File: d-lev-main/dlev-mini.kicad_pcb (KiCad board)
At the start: 4 copper layers, 171.4 x 146.7 mm, 84 parts, among them J1 Conn_01x12_MountingPin, J2 Tag-Connect TC2030-NL, J3 S8B-PH-SM4-TB, J4 S8B-PH-SM4-TB, J5 Conn_01x06_MountingPin, Q2 MMBT3904, Q3 BSS138, Q4 BSS138, Q5 BSS138, SW1 RotaryEncoder_Switch, SW2 RotaryEncoder_Switch, SW3 RotaryEncoder_Switch, SW4 RotaryEncoder_Switch, SW5 RotaryEncoder_Switch, SW6 RotaryEncoder_Switch, SW7 RotaryEncoder_Switch, SW8 RotaryEncoder_Switch, U1 25LCxxx, U2 AMS1117-3.3, U3 AC608

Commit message: many changes to pcb
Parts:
- C10: value .1u -> .01u; footprint Capacitor_SMD:C_0805_2012Metric_Pad1.18x1.45mm_HandSolder -> Capacitor_SMD:C_0603_1608Metric
- C17, C18: value .01u -> 22u; footprint Capacitor_SMD:C_0603_1608Metric -> Capacitor_SMD:C_0805_2012Metric_Pad1.18x1.45mm_HandSolder
- C21: value .01u -> .1u; footprint Capacitor_SMD:C_0603_1608Metric -> Capacitor_SMD:C_0805_2012Metric_Pad1.18x1.45mm_HandSolder
- C7, C8: value 22u -> .01u; footprint Capacitor_SMD:C_0805_2012Metric_Pad1.18x1.45mm_HandSolder -> Capacitor_SMD:C_0603_1608Metric
- DS2: value LCD-20X4B -> LCD-20X4B-noshield
- moved H4 245.4 mm to (-75.5, -98.2)
- moved J2 222.9 mm to (5.00, -106.0), turned to 180 degrees
- moved U1 207.6 mm to (35.0, -67.0), turned to 45 degrees
- moved RV1 199.2 mm to (-54.2, -97.6), turned to 90 degrees
- moved H3 189.3 mm to (75.5, -98.2)
- moved C19 170.9 mm to (-24.0, 104.1)
- moved C9 169.6 mm to (76.0, -44.3)
- moved U2 167.9 mm to (-23.0, -29.0), turned to -135 degrees
- moved C8 166.1 mm to (-41.2, 18.0), turned to 180 degrees
- moved C7 155.7 mm to (-30.3, 18.0)
- moved RN7 153.2 mm to (70.6, -9.95), turned to 90 degrees
- moved C11 152.4 mm to (41.0, -17.0)
- moved H2 144.6 mm to (-75.5, 40.8)
- moved C6 140.7 mm to (-76.0, -9.25), turned to 180 degrees
- moved RN3 139.0 mm to (-70.5, -9.96), turned to 90 degrees
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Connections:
- C10 pad 1: Net-(C10-Pad1) -> enc_6.b
- C11 pad 1: /spdif_tx_1 -> enc_5.a
- C11 pad 2: Net-(C11-Pad2) -> GND
- C12 pad 1: enc_6.a -> enc_5.b
- C13 pad 1: enc_6.b -> enc_7.a
- C14 pad 1: enc_5.a -> enc_7.b
- C15 pad 1: enc_5.b -> enc_8.a
- C16 pad 1: enc_7.a -> enc_8.b
- C17 pad 1: enc_7.b -> +3V3
- C18 pad 1: enc_1.a -> +5V
- C19 pad 1: enc_1.b -> /spdif_tx_1
- C19 pad 2: GND -> Net-(C19-Pad2)
- C20 pad 1: enc_8.a -> /spdif_tx_0
- C20 pad 2: GND -> Net-(C20-Pad2)
- C21 pad 1: enc_8.b -> Net-(C21-Pad1)
- C3 pad 1: enc_3.a -> enc_1.a
- C4 pad 1: enc_3.b -> enc_1.b
- C5 pad 1: enc_4.a -> enc_3.a
- C6 pad 1: enc_4.b -> enc_3.b
- C7 pad 1: +3V3 -> enc_4.a
- C8 pad 1: +5V -> enc_4.b
- C9 pad 1: /spdif_tx_0 -> enc_6.a
- C9 pad 2: Net-(C9-Pad2) -> GND
- R10 pad 1: Net-(C11-Pad2) -> Net-(C19-Pad2)
- R5 pad 1: Net-(C10-Pad1) -> Net-(C21-Pad1)
- R7 pad 2: Net-(C10-Pad1) -> Net-(C21-Pad1)
- R8 pad 2: Net-(C10-Pad1) -> Net-(C21-Pad1)
- R9 pad 1: Net-(C9-Pad2) -> Net-(C20-Pad2)
- RN2 pad 1: /encoder2/B1 -> /encoder/B1
- RN2 pad 2: /encoder2/A1 -> /encoder/A1
- RN2 pad 3: /encoder2/A1 -> /encoder/A1
- RN2 pad 4: /encoder2/B1 -> /encoder/B1
- RN2 pad 7: enc_3.a -> enc_1.a
- RN2 pad 8: enc_3.b -> enc_1.b
- RN3 pad 1: /encoder3/B1 -> /encoder2/B1
- RN3 pad 2: /encoder3/A1 -> /encoder2/A1
- RN3 pad 3: /encoder3/A1 -> /encoder2/A1
- RN3 pad 4: /encoder3/B1 -> /encoder2/B1
- RN3 pad 7: enc_4.a -> enc_3.a
- RN3 pad 8: enc_4.b -> enc_3.b
- RN4 pad 1: /encoder4/B1 -> /encoder3/B1
- RN4 pad 2: /encoder4/A1 -> /encoder3/A1
- RN4 pad 3: /encoder4/A1 -> /encoder3/A1
- RN4 pad 4: /encoder4/B1 -> /encoder3/B1
- RN4 pad 7: enc_6.a -> enc_4.a
- RN4 pad 8: enc_6.b -> enc_4.b
- RN5 pad 1: /encoder7/B1 -> /encoder4/B1
- RN5 pad 2: /encoder7/A1 -> /encoder4/A1
- RN5 pad 3: /encoder7/A1 -> /encoder4/A1
- RN5 pad 4: /encoder7/B1 -> /encoder4/B1
- RN5 pad 7: enc_5.a -> enc_6.a
- RN5 pad 8: enc_5.b -> enc_6.b
- RN6 pad 1: /encoder5/B1 -> /encoder7/B1
- RN6 pad 2: /encoder5/A1 -> /encoder7/A1
- RN6 pad 3: /encoder5/A1 -> /encoder7/A1
- RN6 pad 4: /encoder5/B1 -> /encoder7/B1
- RN6 pad 7: enc_7.a -> enc_5.a
- RN6 pad 8: enc_7.b -> enc_5.b
- RN7 pad 1: /encoder/B1 -> /encoder5/B1
- RN7 pad 2: /encoder/A1 -> /encoder5/A1
- RN7 pad 3: /encoder/A1 -> /encoder5/A1
- RN7 pad 4: /encoder/B1 -> /encoder5/B1
- RN7 pad 7: enc_1.a -> enc_7.a
- RN7 pad 8: enc_1.b -> enc_7.b
- U3 pad 1: (no net) -> unconnected-(U3-IO_T14-Pad1)
- U3 pad 10: (no net) -> unconnected-(U3-IO_L15-Pad10)
- U3 pad 100: (no net) -> unconnected-(U3-IO_R3-Pad100)
- U3 pad 101: (no net) -> unconnected-(U3-IO_T3-Pad101)
- U3 pad 102: (no net) -> unconnected-(U3-IO_R4-Pad102)
- U3 pad 103: (no net) -> unconnected-(U3-IO_T4-Pad103)
- U3 pad 104: (no net) -> unconnected-(U3-IO_R5-Pad104)
- U3 pad 105: (no net) -> unconnected-(U3-IO_T5-Pad105)
- U3 pad 106: (no net) -> +3V3
- U3 pad 107: (no net) -> GND
- U3 pad 108: (no net) -> unconnected-(U3-IO_R6-Pad108)
- U3 pad 109: (no net) -> unconnected-(U3-IO_T6-Pad109)
- U3 pad 11: (no net) -> unconnected-(U3-IO_L16-Pad11)
- U3 pad 110: (no net) -> unconnected-(U3-IO_R7-Pad110)
- U3 pad 111: (no net) -> unconnected-(U3-IO_T7-Pad111)
- U3 pad 112: (no net) -> unconnected-(U3-I_R8-Pad112)
- U3 pad 113: (no net) -> unconnected-(U3-I_T8-Pad113)
- U3 pad 114: (no net) -> unconnected-(U3-I_R9-Pad114)
- U3 pad 115: (no net) -> unconnected-(U3-I_T9-Pad115)
- U3 pad 116: (no net) -> unconnected-(U3-IO_R10-Pad116)
- U3 pad 117: (no net) -> unconnected-(U3-IO_T10-Pad117)
- U3 pad 118: (no net) -> unconnected-(U3-IO_R11-Pad118)
- U3 pad 119: (no net) -> unconnected-(U3-IO_T11-Pad119)
- U3 pad 12: (no net) -> unconnected-(U3-IO_P11-Pad12)
- U3 pad 120: (no net) -> unconnected-(U3-IO_R12-Pad120)
- U3 pad 121: (no net) -> unconnected-(U3-IO_T12-Pad121)
- U3 pad 122: (no net) -> unconnected-(U3-IO_R13-Pad122)
- U3 pad 123: (no net) -> unconnected-(U3-IO_T13-Pad123)
- U3 pad 124: (no net) -> unconnected-(U3-IO_R14-Pad124)
- U3 pad 13: (no net) -> unconnected-(U3-IO_N11-Pad13)
- U3 pad 14: (no net) -> +3V3
- U3 pad 15: (no net) -> GND
- U3 pad 16: (no net) -> unconnected-(U3-IO_N12-Pad16)
- U3 pad 17: (no net) -> unconnected-(U3-IO_P14-Pad17)
- U3 pad 18: (no net) -> unconnected-(U3-IO_N14-Pad18)
- U3 pad 19: (no net) -> unconnected-(U3-IO_L13-Pad19)
- U3 pad 2: (no net) -> unconnected-(U3-IO_T15-Pad2)
- U3 pad 20: (no net) -> unconnected-(U3-IO_K16-Pad20)
- U3 pad 21: (no net) -> unconnected-(U3-IO_J15-Pad21)
- U3 pad 22: (no net) -> unconnected-(U3-IO_J16-Pad22)
- U3 pad 23: (no net) -> unconnected-(U3-IO_L14-Pad23)
- U3 pad 24: (no net) -> unconnected-(U3-IO_J14-Pad24)
- U3 pad 25: (no net) -> unconnected-(U3-IO_K15-Pad25)
- U3 pad 26: (no net) -> unconnected-(U3-IO_F16-Pad26)
- U3 pad 27: (no net) -> unconnected-(U3-IO_G15-Pad27)
- U3 pad 28: (no net) -> unconnected-(U3-IO_F15-Pad28)
- U3 pad 29: (no net) -> unconnected-(U3-I_E16-Pad29)
- U3 pad 3: (no net) -> unconnected-(U3-IO_R16-Pad3)
- U3 pad 30: (no net) -> unconnected-(U3-IO_D16-Pad30)
- U3 pad 31: (no net) -> unconnected-(U3-IO_D15-Pad31)
- U3 pad 32: (no net) -> unconnected-(U3-IO_C16-Pad32)
- U3 pad 33: (no net) -> unconnected-(U3-IO_C15-Pad33)
- U3 pad 34: (no net) -> unconnected-(U3-IO_B16-Pad34)
- U3 pad 35: (no net) -> unconnected-(U3-IO_J13-Pad35)
- U3 pad 36: (no net) -> unconnected-(U3-IO_G16-Pad36)
- U3 pad 37: (no net) -> unconnected-(U3-IO_F8-Pad37)
- U3 pad 38: (no net) -> unconnected-(U3-IO_F13-Pad38)
- U3 pad 39: (no net) -> unconnected-(U3-IO_F14-Pad39)
- U3 pad 4: (no net) -> unconnected-(U3-IO_P15-Pad4)
- U3 pad 40: (no net) -> unconnected-(U3-IO_F9-Pad40)
- U3 pad 41: (no net) -> unconnected-(U3-IO_E11-Pad41)
- U3 pad 42: (no net) -> unconnected-(U3-I_A9-Pad42)
- U3 pad 43: (no net) -> unconnected-(U3-I_B9-Pad43)
- U3 pad 44: (no net) -> unconnected-(U3-IO_C9-Pad44)
- U3 pad 45: (no net) -> unconnected-(U3-I_A8-Pad45)
- U3 pad 46: (no net) -> unconnected-(U3-IO_D9-Pad46)
- U3 pad 47: (no net) -> unconnected-(U3-I_B8-Pad47)
- U3 pad 48: (no net) -> +3V3
- U3 pad 49: (no net) -> GND
- U3 pad 5: (no net) -> unconnected-(U3-IO_P16-Pad5)
- U3 pad 50: (no net) -> unconnected-(U3-I_E1-Pad50)
- U3 pad 51: (no net) -> unconnected-(U3-IO_B1-Pad51)
- U3 pad 52: (no net) -> unconnected-(U3-IO_C2-Pad52)
- U3 pad 53: (no net) -> unconnected-(U3-IO_D1-Pad53)
- U3 pad 54: (no net) -> unconnected-(U3-IO_F3-Pad54)
- U3 pad 55: (no net) -> unconnected-(U3-IO_F2-Pad55)
- U3 pad 56: (no net) -> unconnected-(U3-IO_F1-Pad56)
- U3 pad 57: (no net) -> unconnected-(U3-IO_G5-Pad57)
- U3 pad 58: (no net) -> unconnected-(U3-IO_G2-Pad58)
- U3 pad 59: (no net) -> unconnected-(U3-IO_G1-Pad59)
- U3 pad 6: (no net) -> unconnected-(U3-IO_N15-Pad6)
- U3 pad 60: (no net) -> /FPGA/TCK
- U3 pad 61: (no net) -> /FPGA/TDI
- U3 pad 62: (no net) -> /FPGA/TMS
- U3 pad 63: (no net) -> +2V5
- U3 pad 64: (no net) -> /FPGA/TDO
- U3 pad 65: (no net) -> unconnected-(U3-IO_K5-Pad65)
- U3 pad 66: (no net) -> unconnected-(U3-IO_L4-Pad66)
- U3 pad 67: (no net) -> unconnected-(U3-IO_M6-Pad67)
- U3 pad 68: (no net) -> unconnected-(U3-IO_N3-Pad68)
- U3 pad 69: (no net) -> unconnected-(U3-IO_N5-Pad69)
- U3 pad 7: (no net) -> unconnected-(U3-IO_N16-Pad7)
- U3 pad 70: (no net) -> unconnected-(U3-IO_P3-Pad70)
- U3 pad 71: (no net) -> unconnected-(U3-IO_L7-Pad71)
- U3 pad 72: (no net) -> unconnected-(U3-IO_N6-Pad72)
- U3 pad 73: (no net) -> GND
- U3 pad 74: (no net) -> +1V2
- U3 pad 75: (no net) -> unconnected-(U3-IO_P6-Pad75)
- U3 pad 76: (no net) -> unconnected-(U3-IO_M7-Pad76)
- U3 pad 77: (no net) -> unconnected-(U3-IO_M8-Pad77)
- U3 pad 78: (no net) -> +3V3
- U3 pad 79: (no net) -> GND
- U3 pad 8: (no net) -> unconnected-(U3-I_M15-Pad8)
- U3 pad 80: (no net) -> unconnected-(U3-IO_P8-Pad80)
- U3 pad 81: (no net) -> unconnected-(U3-IO_N8-Pad81)
- U3 pad 82: (no net) -> unconnected-(U3-IO_L8-Pad82)
- U3 pad 83: (no net) -> unconnected-(U3-IO_N9-Pad83)
- U3 pad 84: (no net) -> unconnected-(U3-IO_P9-Pad84)
- U3 pad 85: (no net) -> unconnected-(U3-IO_M10-Pad85)
- U3 pad 86: (no net) -> unconnected-(U3-LVDS_TX1_N-Pad86)
- U3 pad 87: (no net) -> unconnected-(U3-LVDS_TX1_P-Pad87)
- U3 pad 88: (no net) -> unconnected-(U3-LVDS_TX2_N-Pad88)
- U3 pad 89: (no net) -> unconnected-(U3-LVDS_TX2_P-Pad89)
- U3 pad 9: (no net) -> unconnected-(U3-I_M16-Pad9)
- U3 pad 90: (no net) -> unconnected-(U3-LVDS_TX3_N-Pad90)
- U3 pad 91: (no net) -> unconnected-(U3-LVDS_TX3_P-Pad91)
- U3 pad 92: (no net) -> unconnected-(U3-LVDS_RXCLK_N-Pad92)
- U3 pad 93: (no net) -> unconnected-(U3-LVDS_RXCLK_P-Pad93)
- U3 pad 94: (no net) -> unconnected-(U3-LVDS_TX4_N-Pad94)
- U3 pad 95: (no net) -> unconnected-(U3-LVDS_TX4_P-Pad95)
- U3 pad 96: (no net) -> unconnected-(U3-LVDS_TX5_N-Pad96)
- U3 pad 97: (no net) -> unconnected-(U3-LVDS_TX5_P-Pad97)
- U3 pad 98: (no net) -> unconnected-(U3-IO_R1-Pad98)
- U3 pad 99: (no net) -> unconnected-(U3-IO_T2-Pad99)
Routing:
- net /encoder3/B1: track 0.00 -> 9.17 mm
- net /encoder5/B1: track 0.00 -> 9.17 mm
- net /encoder/B1: track 0.00 -> 9.17 mm
- net /encoder4/B1: track 0.00 -> 9.17 mm
- net /encoder2/B1: track 0.00 -> 9.17 mm
- net /encoder6/B1: track 0.00 -> 9.17 mm
- net /encoder7/B1: track 0.00 -> 9.17 mm
- net enc_8.a: track 0.00 -> 6.72 mm
- net enc_5.a: track 0.00 -> 6.72 mm
- net enc_6.a: track 0.00 -> 6.72 mm
- net enc_4.a: track 0.00 -> 6.72 mm
- net enc_3.a: track 0.00 -> 6.72 mm
- net enc_7.a: track 0.00 -> 6.72 mm
- net enc_1.a: track 0.00 -> 6.72 mm
- net /encoder2/A1: track 0.00 -> 6.46 mm
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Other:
- board size 171.4 x 146.7 mm -> 175.3 x 163.3 mm

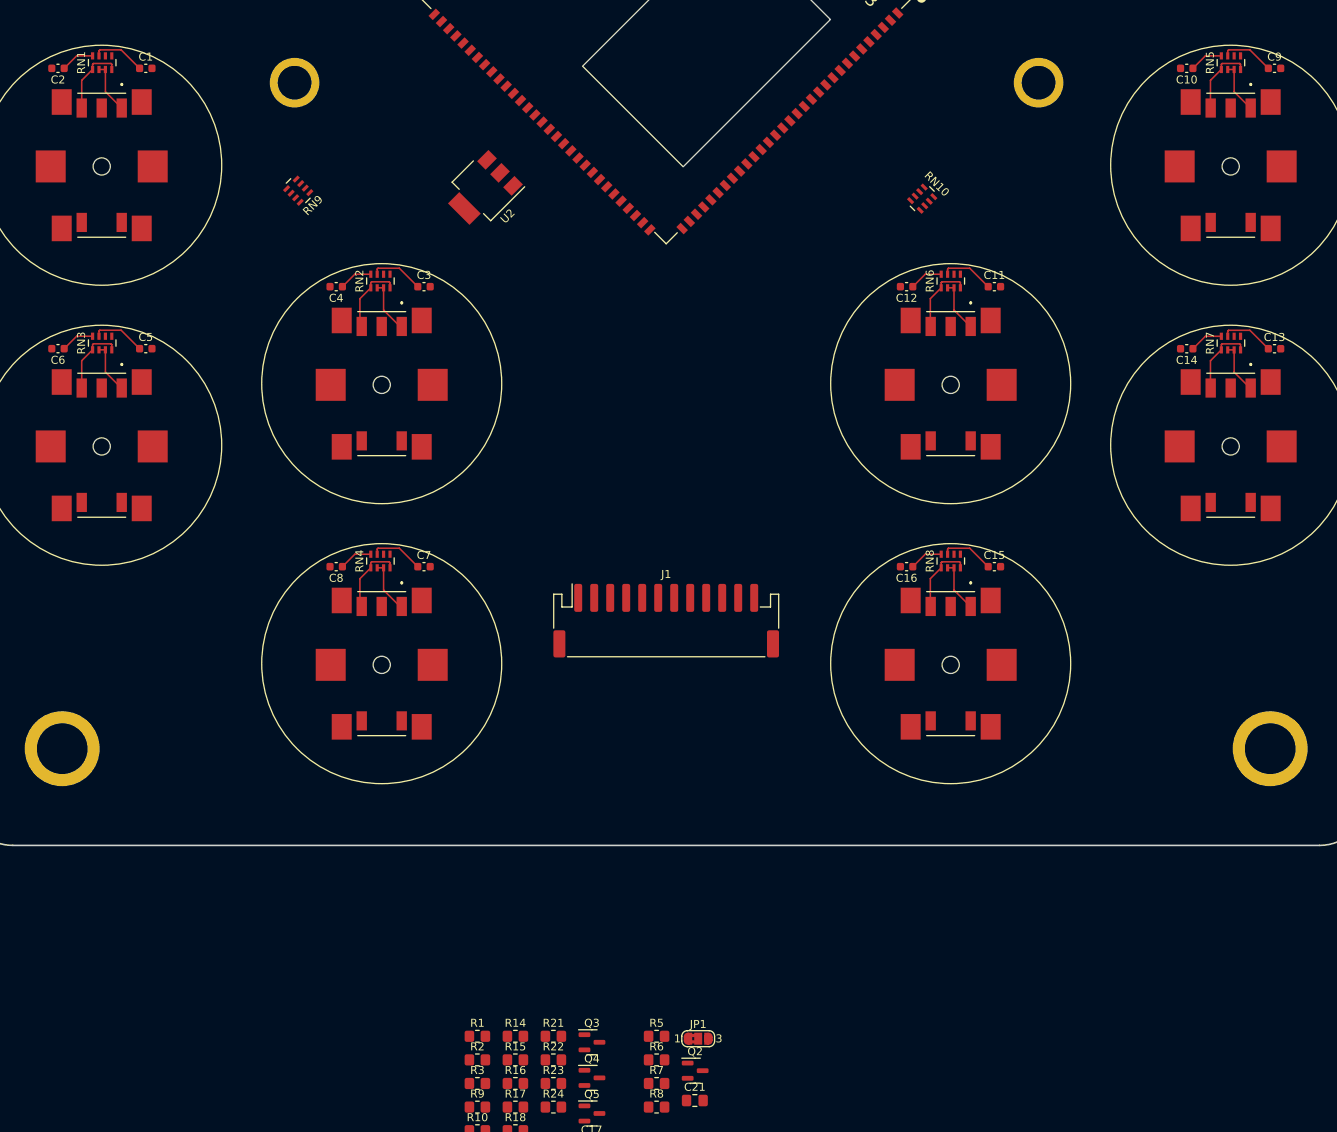
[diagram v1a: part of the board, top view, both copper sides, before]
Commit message: Switch from Rpacks to 0603 pull resistors
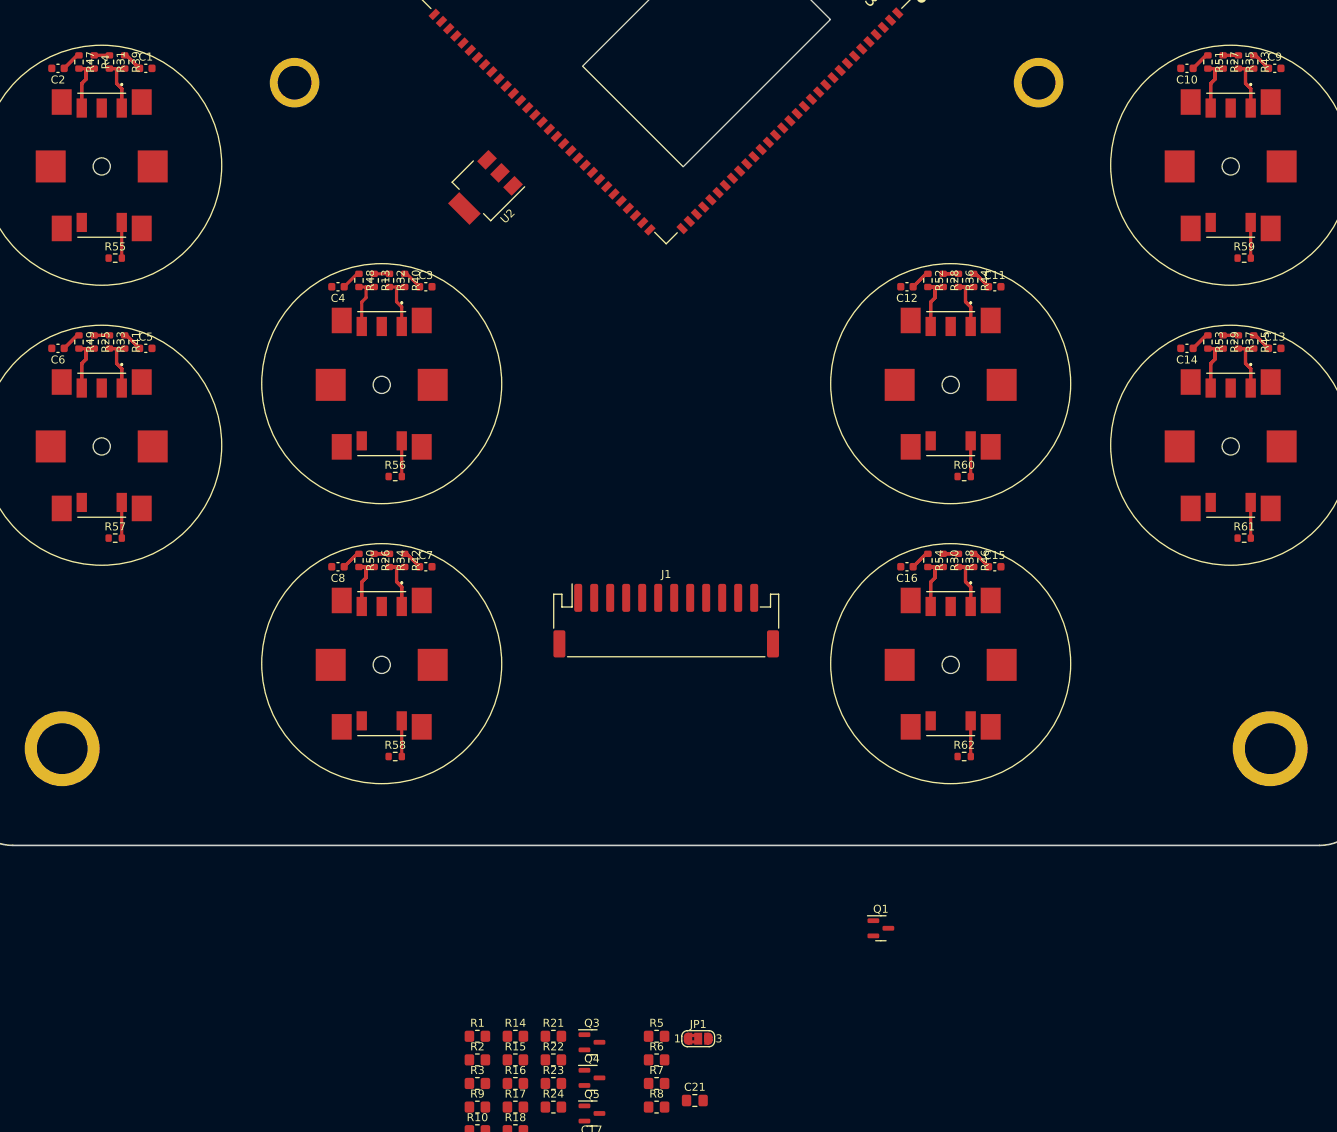
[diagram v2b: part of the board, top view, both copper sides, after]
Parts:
- removed Q2: MMBT3904, Package_TO_SOT_SMD:SOT-23
- removed RN1, RN10, RN2, RN3, RN4, RN5, RN6, RN7, RN8, RN9: 4.7k, Resistor_SMD:R_Array_Concave_4x0603
- added Q1: BSS138, Package_TO_SOT_SMD:SOT-23, F.Cu at (26.8, 63.2)
- added R13: R_Small, Resistor_SMD:R_0603_1608Metric, F.Cu at (-36.5, -17.8)
- added R25: R_Small, Resistor_SMD:R_0603_1608Metric, F.Cu at (-71.5, -10.1)
- added R26: R_Small, Resistor_SMD:R_0603_1608Metric, F.Cu at (-36.5, 17.2)
- added R27: R_Small, Resistor_SMD:R_0603_1608Metric, F.Cu at (69.6, -45.1)
- added R28: R_Small, Resistor_SMD:R_0603_1608Metric, F.Cu at (34.6, -17.8)
- added R29: R_Small, Resistor_SMD:R_0603_1608Metric, F.Cu at (69.6, -10.1)
- added R30: R_Small, Resistor_SMD:R_0603_1608Metric, F.Cu at (34.6, 17.2)
- added R31: R_Small, Resistor_SMD:R_0603_1608Metric, F.Cu at (-69.6, -45.1)
- added R32: R_Small, Resistor_SMD:R_0603_1608Metric, F.Cu at (-34.6, -17.8)
- added R33: R_Small, Resistor_SMD:R_0603_1608Metric, F.Cu at (-69.6, -10.1)
- added R34: R_Small, Resistor_SMD:R_0603_1608Metric, F.Cu at (-34.6, 17.2)
- added R35: R_Small, Resistor_SMD:R_0603_1608Metric, F.Cu at (71.5, -45.1)
- added R36: R_Small, Resistor_SMD:R_0603_1608Metric, F.Cu at (36.5, -17.8)
- added R37: R_Small, Resistor_SMD:R_0603_1608Metric, F.Cu at (71.5, -10.1)
- added R38: R_Small, Resistor_SMD:R_0603_1608Metric, F.Cu at (36.5, 17.2)
- added R39: R_Small, Resistor_SMD:R_0603_1608Metric, F.Cu at (-67.7, -45.1)
- added R4: R_Small, Resistor_SMD:R_0603_1608Metric, F.Cu at (-71.5, -45.1)
- added R40: R_Small, Resistor_SMD:R_0603_1608Metric, F.Cu at (-32.7, -17.8)
- added R41: R_Small, Resistor_SMD:R_0603_1608Metric, F.Cu at (-67.7, -10.1)
- added R42: R_Small, Resistor_SMD:R_0603_1608Metric, F.Cu at (-32.7, 17.2)
- added R43: R_Small, Resistor_SMD:R_0603_1608Metric, F.Cu at (73.4, -45.1)
- added R44: R_Small, Resistor_SMD:R_0603_1608Metric, F.Cu at (38.4, -17.8)
- added R45: R_Small, Resistor_SMD:R_0603_1608Metric, F.Cu at (73.4, -10.1)
- added R46: R_Small, Resistor_SMD:R_0603_1608Metric, F.Cu at (38.4, 17.2)
- added R47: R_Small, Resistor_SMD:R_0603_1608Metric, F.Cu at (-73.4, -45.1)
- added R48: R_Small, Resistor_SMD:R_0603_1608Metric, F.Cu at (-38.4, -17.8)
- added R49: R_Small, Resistor_SMD:R_0603_1608Metric, F.Cu at (-73.4, -10.1)
- added R50: R_Small, Resistor_SMD:R_0603_1608Metric, F.Cu at (-38.4, 17.2)
- added R51: R_Small, Resistor_SMD:R_0603_1608Metric, F.Cu at (67.7, -45.1)
- added R52: R_Small, Resistor_SMD:R_0603_1608Metric, F.Cu at (32.7, -17.8)
- added R53: R_Small, Resistor_SMD:R_0603_1608Metric, F.Cu at (67.7, -10.1)
- added R54: R_Small, Resistor_SMD:R_0603_1608Metric, F.Cu at (32.7, 17.2)
- added R55: R_Small, Resistor_SMD:R_0603_1608Metric, F.Cu at (-68.9, -20.6)
- added R56: R_Small, Resistor_SMD:R_0603_1608Metric, F.Cu at (-33.9, 6.73)
- added R57: R_Small, Resistor_SMD:R_0603_1608Metric, F.Cu at (-68.9, 14.4)
- added R58: R_Small, Resistor_SMD:R_0603_1608Metric, F.Cu at (-33.9, 41.7)
- added R59: R_Small, Resistor_SMD:R_0603_1608Metric, F.Cu at (72.2, -20.6)
- added R60: R_Small, Resistor_SMD:R_0603_1608Metric, F.Cu at (37.2, 6.73)
- added R61: R_Small, Resistor_SMD:R_0603_1608Metric, F.Cu at (72.2, 14.4)
- added R62: R_Small, Resistor_SMD:R_0603_1608Metric, F.Cu at (37.2, 41.7)
- moved C4 0.22 mm to (-41.0, -17.0)
- moved C8 0.22 mm to (-41.0, 18.0)
- moved C3 0.22 mm to (-30.1, -17.0)
- moved C7 0.22 mm to (-30.1, 18.0)
- moved C13 0.06 mm to (76.1, -9.29)
- moved C14 0.06 mm to (65.1, -9.29)
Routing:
- net +3V3: track 0.00 -> 28.6 mm
- net /encoder4/A1: track 6.46 -> 14.2 mm
- net /encoder5/A1: track 6.46 -> 14.2 mm
- net /encoder7/A1: track 6.46 -> 14.2 mm
- net /encoder6/A1: track 6.46 -> 14.2 mm
- net /encoder3/A1: track 6.46 -> 14.2 mm
- net /encoder1/A1: track 6.46 -> 14.2 mm
- net /encoder2/A1: track 6.46 -> 14.2 mm
- net /encoder1/B1: track 9.17 -> 14.1 mm
- net /encoder2/B1: track 9.17 -> 14.1 mm
- net /encoder7/B1: track 9.17 -> 14.1 mm
- net /encoder6/B1: track 9.17 -> 14.1 mm
- net /encoder3/B1: track 9.17 -> 14.1 mm
- net /encoder4/B1: track 9.17 -> 14.1 mm
- net /encoder5/B1: track 9.17 -> 14.1 mm
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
